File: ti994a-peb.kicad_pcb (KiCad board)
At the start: 2 copper layers, 237.7 x 146.1 mm, 24 parts, among them Q1 Q_NPN_BCE, U1 74HCT138, U2 L7805, U3 74HCT244, U4 74HCT244, U5 74HCT244, U7 74HCT245

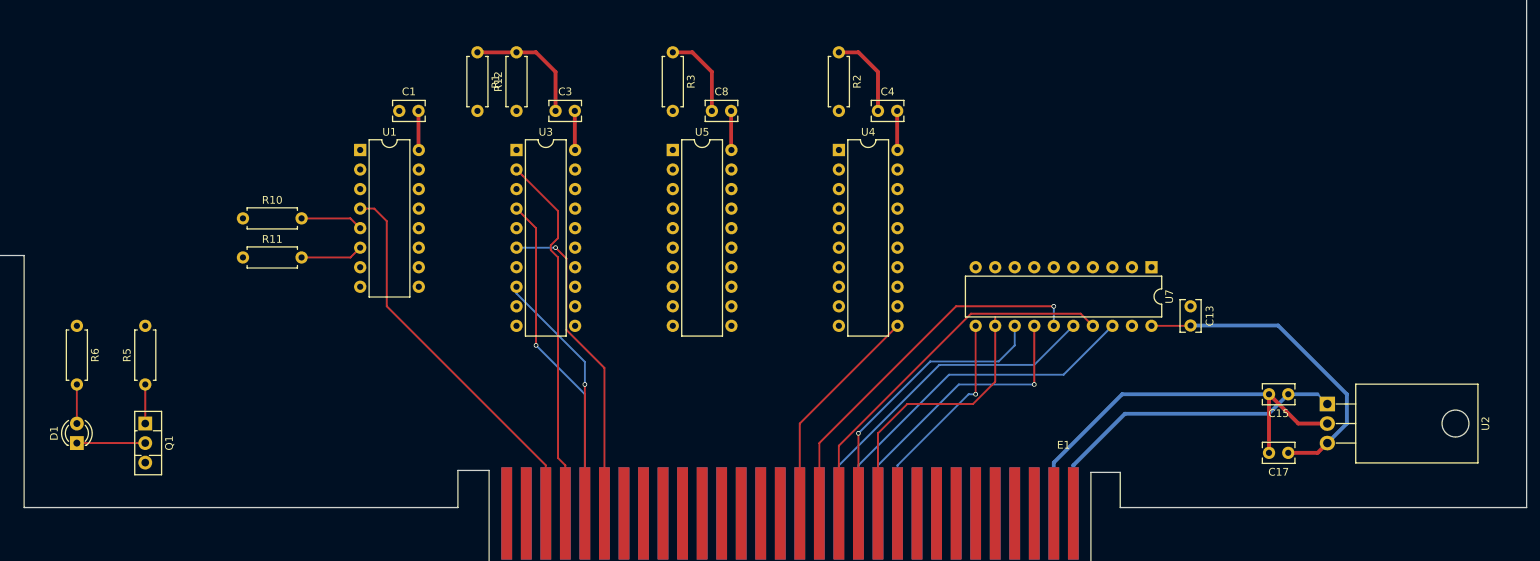
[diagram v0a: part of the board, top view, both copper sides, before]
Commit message: cleanup all outdated parts
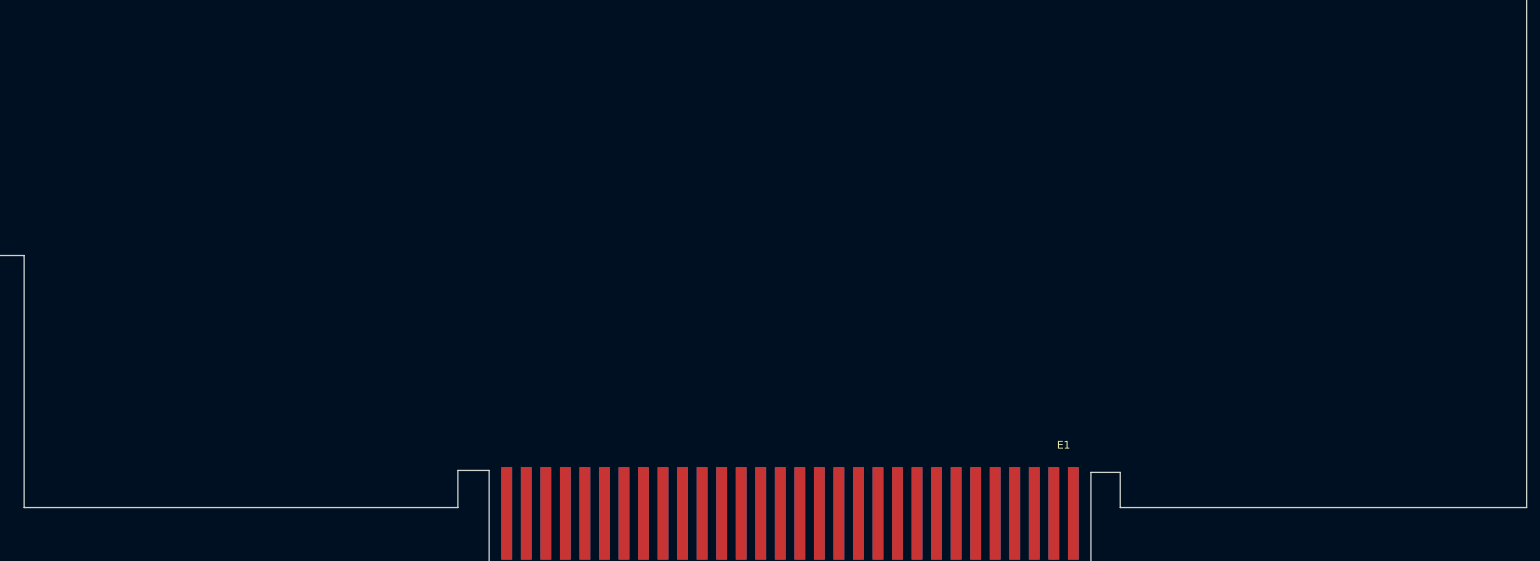
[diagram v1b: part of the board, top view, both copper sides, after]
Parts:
- removed C1, C13, C3, C4, C8: 0.1uf, Capacitor_THT:C_Rect_L4.0mm_W2.5mm_P2.50mm
- removed C15: 10uf, Capacitor_THT:C_Rect_L4.0mm_W2.5mm_P2.50mm
- removed C17: 22uf, Capacitor_THT:C_Rect_L4.0mm_W2.5mm_P2.50mm
- removed D1: LED_ALT, LED_THT:LED_D3.0mm
- removed Q1: Q_NPN_BCE, Package_TO_SOT_THT:TO-126-3_Vertical
- removed R1, R10, R12, R2, R3, R5: 1k, Resistor_THT:R_Axial_DIN0207_L6.3mm_D2.5mm_P7.62mm_Horizontal
- removed R11: 10k, Resistor_THT:R_Axial_DIN0207_L6.3mm_D2.5mm_P7.62mm_Horizontal
- removed R6: 330, Resistor_THT:R_Axial_DIN0207_L6.3mm_D2.5mm_P7.62mm_Horizontal
- removed U1: 74HCT138, Package_DIP:DIP-16_W7.62mm
- removed U2: L7805, Package_TO_SOT_THT:TO-220-3_Horizontal_TabDown
- removed U3, U4, U5: 74HCT244, Package_DIP:DIP-20_W7.62mm
- removed U7: 74HCT245, Package_DIP:DIP-20_W7.62mm
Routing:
- net GND: track 104.3 -> 10.5 mm
- net +5V: track 62.5 -> 0.00 mm
- net TI_MEMEN: track 50.7 -> 0.00 mm
- net TI_D2: track 54.8 -> 5.20 mm
- net TI_D0: track 49.5 -> 0.00 mm, vias 1 -> 0
- net TI_WE: track 48.1 -> 0.00 mm
- net TI_D3: track 46.8 -> 0.00 mm
- net TI_D1: track 44.2 -> 0.00 mm
- net +8V: track 43.6 -> 0.00 mm
- net TI_CRUCLK: track 43.3 -> 0.00 mm, vias 1 -> 0
- net TI_PH3: track 42.3 -> 0.00 mm, vias 1 -> 0
- net TI_D5: track 38.5 -> 0.00 mm, vias 1 -> 0
- net TI_D4: track 38.0 -> 0.00 mm, vias 1 -> 0
- net TI_D6: track 42.0 -> 5.20 mm
- net TI_DBIN: track 33.1 -> 0.00 mm, vias 1 -> 0
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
